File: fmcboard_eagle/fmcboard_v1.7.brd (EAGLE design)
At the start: 147 x 74 mm, 294 parts, among them IC1 OPA699ID, IC10 LM358, IC11 7805DT, IC12 SN74AUC2G66DCTR, IC13 SN74AUC2G66DCTR, IC14 SN74AUC2G66DCTR, IC15 SN74AUC2G66DCTR, IC16 DAC7578SPWR, IC17 SN74AUC2G66DCTR, IC18 SN74AUC2G66DCTR, IC19 SN74AUC2G66DCTR, IC2 DAC7578SPWR, IC20 SN74AUC2G66DCTR, IC21 74AUP2GU04GW, IC22 74AUP2GU04GW, IC23 74AUP2GU04GW, IC24 74AUP2GU04GW, IC25 MC7905ACD2TR4G, IC26 AMS1117-1.8, IC27 LM358, IC28 SN74AUC2G66DCTR, IC29 LM337KVURG3, IC3 LTC6229IMS8E#TRPBF, IC30 SN74AUC2G66DCTR, IC31 SN74AUC2G66DCTR, IC32 SN74AUC2G66DCTR, IC33 LTC6229IMS8E#TRPBF, IC34 74AUP2GU04GW, IC35 74AUP2GU04GW, IC36 TPS5430DDAR, IC37 TPS5430DDAR, IC38 LTC6229IMS8E#TRPBF, IC4 OPA695IDR, IC5 LTC6229IMS8E#TRPBF, IC6 OPA695IDR, IC7 OPA699ID, IC8 LM358, IC9 LM358, J1 4p-2.54, J13 4p-2.54, J2 ASP-134604-01, J3 2X4P-2.54, J4 2X4P-2.54, J5 4p-2.54

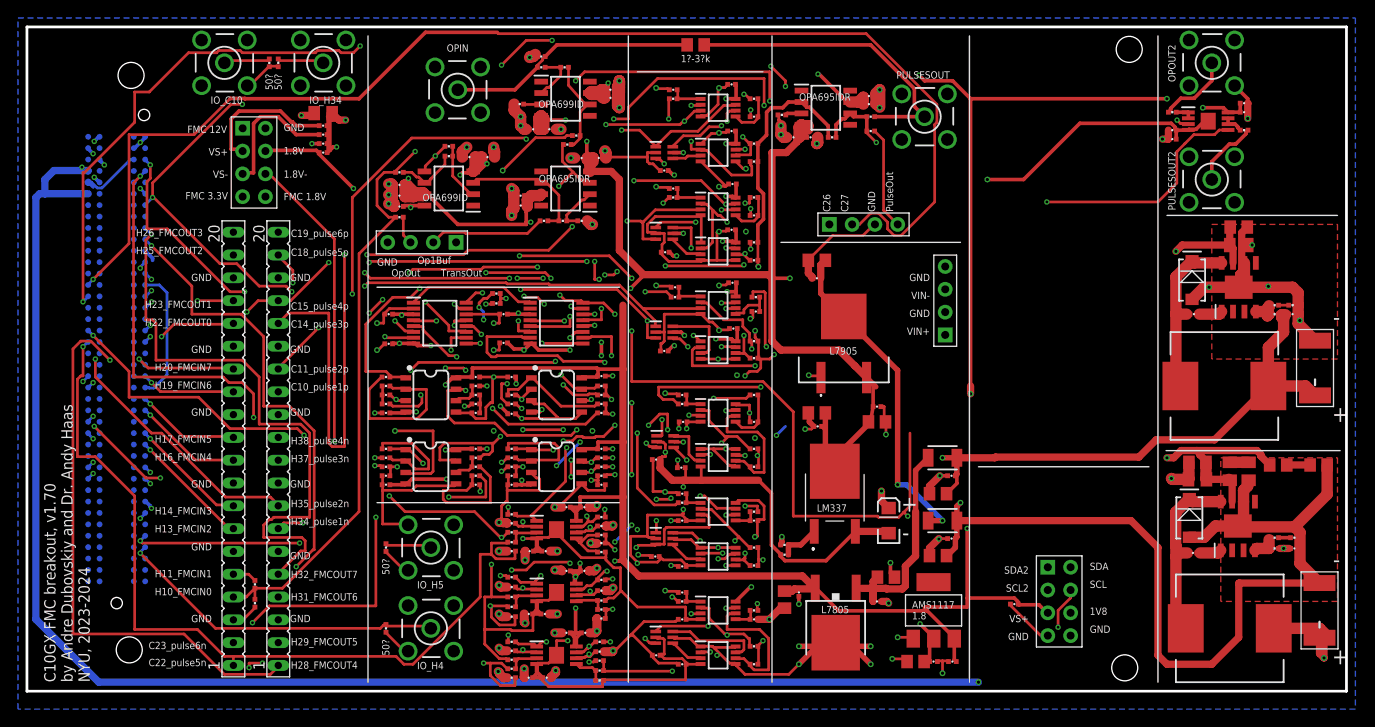
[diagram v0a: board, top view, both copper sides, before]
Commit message: add level shifting
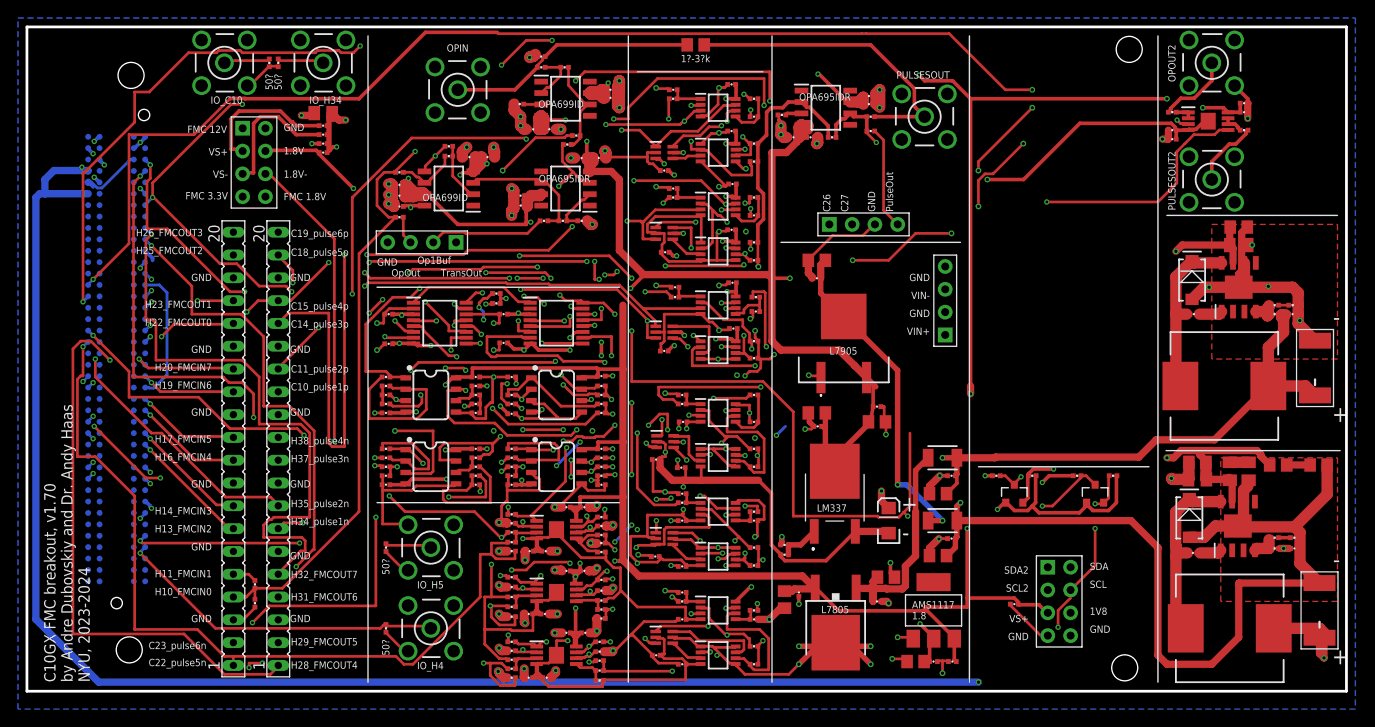
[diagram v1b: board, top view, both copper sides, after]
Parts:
- added R48, R49, R50, R51: 10k, passives:0402_RES
- added U$1, U$2: N-CHANNEL-MOSFET-BSS138, GeekAmmo:SOT23-3
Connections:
- removed net AR_SCLIN2: IC16.16, IC2.16, J4.2
- removed net AR_SDAIN2: IC16.15, IC2.15, J4.1
- new net SCLIN2: IC16.16, IC2.16, J4.2, R51.2, U$2.3
- new net SDAIN2: IC16.15, IC2.15, J4.1, R49.2, U$1.3
- net 1V8: now also R48.1, R50.1, U$1.1, U$2.1
- net SCLIN: now also R50.2, U$2.2
- net SDAIN: now also R48.2, U$1.2
- net VS+: now also R49.1, R51.1
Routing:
- net SDAIN2: track 0.00 -> 142.1 mm, vias 0 -> 5
- net AR_SDAIN2: track 135.9 -> 0.00 mm, vias 4 -> 0
- net SCLIN2: track 0.00 -> 119.7 mm, vias 0 -> 8
- net AR_SCLIN2: track 100.5 -> 0.00 mm, vias 7 -> 0
- net C26: track 121.3 -> 163.9 mm, vias 4 -> 6
- net 1V8: track 227.5 -> 267.8 mm, vias 20 -> 21
- net SDAIN: track 127.5 -> 145.7 mm, vias 1 -> 2
- net C27: track 140.4 -> 155.8 mm, vias 1 -> 4
- net SCLIN: track 123.9 -> 138.9 mm, vias 4 -> 6
- net VS+: track 421.7 -> 436.5 mm, vias 17 -> 19

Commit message: caps
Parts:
- added C118: 0.1uF, passives:0402_CAP
- moved C6 12.6 mm to (107.3, 22.0), turned to 270 degrees
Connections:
- net 1V8: now also C118.1
- net GND: now also C118.2
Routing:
- net GND: track 547.7 -> 544.3 mm, vias 126 -> 128
- net 1V8: track 267.8 -> 269.7 mm
- net VS+: track 436.5 -> 437.7 mm
- net SCLIN: track 138.9 -> 139.5 mm
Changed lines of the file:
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@@
 <attribute name="OC_NEWARK" value="unknown" x="100" y="64" size="0.8128" layer="27" display="off"/>
 </element>
-<element name="C6" library="passives" package="0402_CAP" value="0.1uF" x="110" y="9.7" smashed="yes" rot="R180"/>
+<element name="C6" library="passives" package="0402_CAP" value="0.1uF" x="107.3" y="22" smashed="yes" rot="R270"/>
 <element name="C15" library="passives" package="0402_CAP" value="0.1uF" x="54" y="35" smashed="yes" rot="R180"/>
 <element name="C16" library="passives" package="0402_CAP" value="0.1uF" x="93.8" y="66.3" smashed="yes"/>
@@
 <element name="R50" library="passives" package="0402_RES" value="10k" x="121" y="24" smashed="yes" rot="R180"/>
 <element name="R51" library="passives" package="0402_RES" value="10k" x="117" y="24" smashed="yes"/>
+<element name="C118" library="passives" package="0402_CAP" value="0.1uF" x="123" y="22" smashed="yes" rot="R270"/>
 </elements>
 <signals>
@@
 <contactref element="J4" pad="4"/>
 <contactref element="J4" pad="5"/>
-<wire x1="109.625" y1="9.5" x2="109.625" y2="9.625" width="0.3048" layer="1"/>
-<wire x1="112.875" y1="6.25" x2="109.625" y2="9.5" width="0.3048" layer="1"/>
-<wire x1="113.625" y1="6.25" x2="112.875" y2="6.25" width="0.3048" layer="1"/>
-<wire x1="109.625" y1="9.625" x2="109.56693125" y2="9.7" width="0.3048" layer="1"/>
-<wire x1="113.625" y1="6.25" x2="113.73" y2="6.19" width="0.3048" layer="1"/>
 <wire x1="89.75" y1="50.75" x2="87.25" y2="48.25" width="0.3048" layer="1"/>
 <wire x1="93.125" y1="50.75" x2="89.75" y2="50.75" width="0.3048" layer="1"/>
@@
 <wire x1="87.25" y1="48.25" x2="87.05" y2="48" width="0.3048" layer="1"/>
 <wire x1="94.375" y1="52" x2="94.47" y2="52" width="0.3048" layer="1"/>
+<contactref element="C118" pad="2"/>
+<via x="122.5" y="20.7" extent="1-16" drill="0.35"/>
+<via x="106.5" y="20.7" extent="1-16" drill="0.35"/>
+<wire x1="106.5" y1="20.7" x2="107.3" y2="21.5" width="0.4064" layer="1"/>
+<wire x1="107.3" y1="21.5" x2="107.3" y2="21.56693125" width="0.4064" layer="1"/>
+<wire x1="122.5" y1="20.7" x2="123" y2="21.2" width="0.4064" layer="1"/>
+<wire x1="123" y1="21.2" x2="123" y2="21.56693125" width="0.4064" layer="1"/>
 </signal>
 <signal name="IO1">
@@
 <wire x1="26.65" y1="60.25" x2="32.25" y2="60.25" width="0.4064" layer="1"/>
 <contactref element="J4" pad="6"/>
-<wire x1="115.125" y1="8.625" x2="116.25" y2="8.625" width="0.4064" layer="15"/>
-<wire x1="114.125" y1="7.625" x2="115.125" y2="8.625" width="0.4064" layer="15"/>
-<wire x1="99.625" y1="7.625" x2="114.125" y2="7.625" width="0.4064" layer="15"/>
+<wire x1="115.425" y1="8.625" x2="116.25" y2="8.625" width="0.4064" layer="15"/>
+<wire x1="114.325" y1="7.525" x2="115.425" y2="8.625" width="0.4064" layer="15"/>
+<wire x1="99.525" y1="7.525" x2="114.325" y2="7.525" width="0.4064" layer="15"/>
 <wire x1="116.25" y1="8.625" x2="116.27" y2="8.73" width="0.4064" layer="15"/>
-<wire x1="99.625" y1="7.625" x2="99.5" y2="7.5" width="0.4064" layer="15"/>
+<wire x1="99.525" y1="7.525" x2="99.5" y2="7.5" width="0.4064" layer="15"/>
 <contactref element="R48" pad="1"/>
 <contactref element="U$1" pad="1"/>
@@
 <wire x1="112.375" y1="24" x2="112.43306875" y2="24" width="0.4064" layer="1"/>
 <wire x1="109.125" y1="21" x2="109.05" y2="21" width="0.4064" layer="1"/>
-<wire x1="121.375" y1="21" x2="121.375" y2="24" width="0.4064" layer="1"/>
+<wire x1="121.375" y1="21" x2="121.375" y2="23" width="0.4064" layer="1"/>
+<wire x1="121.375" y1="23" x2="121.375" y2="24" width="0.4064" layer="1"/>
 <wire x1="120.5" y1="20.125" x2="121.375" y2="21" width="0.4064" layer="1"/>
 <wire x1="118.75" y1="20.125" x2="120.5" y2="20.125" width="0.4064" layer="1"/>
@@
 <wire x1="93" y1="20.25" x2="92.875" y2="20.125" width="0.4064" layer="15"/>
 <via x="108.125" y="20.25" extent="1-16" drill="0.3048"/>
+<contactref element="C118" pad="1"/>
+<wire x1="123" y1="22.43306875" x2="121.94193125" y2="22.43306875" width="0.4064" layer="1"/>
+<wire x1="121.94193125" y1="22.43306875" x2="121.375" y2="23" width="0.4064" layer="1"/>
 </signal>
 <signal name="3V3" class="1" airwireshidden="yes">
@@
 <wire x1="104.85" y1="23.125" x2="104.85" y2="24" width="0.4064" layer="15"/>
 <wire x1="104.85" y1="24" x2="104.85" y2="32.85" width="0.4064" layer="15"/>
-<wire x1="104.75" y1="9.375" x2="104.75" y2="10.375" width="0.4064" layer="1"/>
-<wire x1="104.75" y1="10.375" x2="104.75" y2="18.125" width="0.4064" layer="1"/>
+<wire x1="104.75" y1="9.375" x2="104.75" y2="18.125" width="0.4064" layer="1"/>
 <wire x1="100.125" y1="9.375" x2="104.75" y2="9.375" width="0.4064" layer="1"/>
 <wire x1="100.125" y1="9.375" x2="100" y2="9.25" width="0.4064" layer="1"/>
@@
 <wire x1="24" y1="60.2" x2="24" y2="60.375" width="0.4064" layer="1"/>
 <contactref element="J4" pad="3"/>
-<wire x1="112.75" y1="9.625" x2="110.5" y2="9.625" width="0.4064" layer="1"/>
-<wire x1="113.625" y1="8.75" x2="112.75" y2="9.625" width="0.4064" layer="1"/>
-<wire x1="110.5" y1="9.625" x2="110.43306875" y2="9.7" width="0.4064" layer="1"/>
-<wire x1="113.625" y1="8.75" x2="113.73" y2="8.73" width="0.4064" layer="1"/>
-<wire x1="110.375" y1="10" x2="110.375" y2="9.875" width="0.4064" layer="1"/>
-<wire x1="110" y1="10.375" x2="110.375" y2="10" width="0.4064" layer="1"/>
-<wire x1="104.75" y1="10.375" x2="110" y2="10.375" width="0.4064" layer="1"/>
-<wire x1="110.375" y1="9.875" x2="110.43306875" y2="9.7" width="0.4064" layer="1"/>
 <contactref element="R49" pad="1"/>
 <contactref element="R51" pad="1"/>
@@
 <via x="106.75" y="24" extent="1-16" drill="0.3048"/>
 <via x="113.125" y="23.25" extent="1-16" drill="0.3048"/>
+<wire x1="113.73" y1="8.73" x2="105.395" y2="8.73" width="0.4064" layer="1"/>
+<wire x1="105.395" y1="8.73" x2="104.75" y2="9.375" width="0.4064" layer="1"/>
+<wire x1="107.3" y1="22.43306875" x2="107.56693125" y2="22.7" width="0.4064" layer="1"/>
+<wire x1="107.56693125" y1="22.7" x2="107.56693125" y2="24" width="0.4064" layer="1"/>
 </signal>
 <signal name="VS-" class="1" airwireshidden="yes">
@@
 <wire x1="114.875" y1="9" x2="116.25" y2="10.375" width="0.3048" layer="1"/>
 <wire x1="114.875" y1="7.125" x2="114.875" y2="9" width="0.3048" layer="1"/>
-<wire x1="114.875" y1="5.875" x2="114.875" y2="7.125" width="0.3048" layer="15"/>
-<wire x1="112.375" y1="3.375" x2="114.875" y2="5.875" width="0.3048" layer="15"/>
-<wire x1="99.375" y1="3.375" x2="112.375" y2="3.375" width="0.3048" layer="15"/>
+<wire x1="114.875" y1="4.875" x2="114.875" y2="7.125" width="0.3048" layer="15"/>
+<wire x1="113.375" y1="3.375" x2="114.875" y2="4.875" width="0.3048" layer="15"/>
+<wire x1="99.375" y1="3.375" x2="113.375" y2="3.375" width="0.3048" layer="15"/>
 <wire x1="97.5" y1="1.5" x2="99.375" y2="3.375" width="0.3048" layer="15"/>
 <wire x1="116.25" y1="11.25" x2="116.27" y2="11.27" width="0.3048" layer="1"/>
@@
 <wire x1="139.8001" y1="41.93955" x2="140.1999" y2="41.93955" width="1.27" layer="1"/>
 <wire x1="138.3" y1="34" x2="132.3" y2="28" width="0.8128" layer="1"/>
-<wire x1="107.90000625" y1="26.0788" x2="107.82120625" y2="26" width="0.8128" layer="1"/>
-<wire x1="107.82120625" y1="26" x2="103.6" y2="26" width="0.8128" layer="1"/>
-<wire x1="123.87759375" y1="26.0788" x2="107.90000625" y2="26.0788" width="0.8128" layer="1"/>
+<wire x1="123.79879375" y1="26" x2="103.6" y2="26" width="0.8128" layer="1"/>
 <wire x1="132.3" y1="28" x2="125.79879375" y2="28" width="0.8128" layer="1"/>
-<wire x1="125.79879375" y1="28" x2="123.87759375" y2="26.0788" width="0.8128" layer="1"/>
+<wire x1="125.79879375" y1="28" x2="123.79879375" y2="26" width="0.8128" layer="1"/>
 <wire x1="139.5" y1="42" x2="139.43306875" y2="42" width="0.4064" layer="1"/>
 <wire x1="139.5" y1="42" x2="139.8001" y2="41.63296875" width="0.4064" layer="1"/>

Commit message: compress board
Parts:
- J4: value 2X4P-2.54 -> 4p-2.54; device Seeed-Connector:H2X4-2.54 -> Seeed-Connector:H4-2.54
- moved J4 125.5 mm to (5.80, 71.9), turned to 90 degrees
- moved C118 88.1 mm to (35.7, 10.4), turned to 0 degrees
- moved R50 87.7 mm to (34.4, 9.90), turned to 270 degrees
- moved U$2 84.4 mm to (35.7, 8.40), turned to 90 degrees
- moved R51 84.4 mm to (34.4, 6.90), turned to 90 degrees
- moved R48 79.9 mm to (34.4, 5.10), turned to 270 degrees
- moved R49 76.8 mm to (34.4, 2.00), turned to 90 degrees
- moved U$1 76.5 mm to (35.7, 3.60), turned to 90 degrees
- moved C6 74.5 mm to (35.7, 1.50), turned to 0 degrees
- moved D1 20.0 mm to (109.8, 45.8)
- moved C107 20.0 mm to (109.9, 15.4)
- moved C108 20.0 mm to (114.0, 24.5)
- moved C109 20.0 mm to (123.9, 25.2)
- moved C11 20.0 mm to (110.4, 23.6)
- moved C112 20.0 mm to (119.4, 25.2)
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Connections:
- net 1V8: no longer J4.6
- net C26: now also J4.1; no longer J13.1
- net C27: now also J4.3; no longer J13.2
- net GND: now also J13.1, J13.2, J4.2; no longer J4.5
- net SCLIN: no longer J4.7
- net SCLIN2: no longer J4.2
- net SDAIN: no longer J4.8
- net SDAIN2: no longer J4.1
- net VS+: no longer J4.3
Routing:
- net C26: track 163.9 -> 31.2 mm, vias 6 -> 1
- net C27: track 155.8 -> 27.3 mm, vias 4 -> 1
- net SDAIN: track 145.7 -> 33.0 mm
- net SCLIN: track 139.5 -> 39.1 mm, vias 6 -> 4
- net SCLIN2: track 119.7 -> 164.5 mm, vias 8 -> 7
- net VS+: track 437.7 -> 393.0 mm, vias 19 -> 18
- net GND: track 544.3 -> 508.7 mm, vias 128 -> 125
- net C14: track 127.8 -> 94.5 mm
- net PULSESUMOUT: track 56.2 -> 31.0 mm
- net VIN+: track 73.9 -> 53.9 mm
- net VS-: track 302.6 -> 283.6 mm
- net VIN-: track 126.7 -> 108.9 mm
- net OPOUT_H10: track 180.2 -> 162.6 mm
- net SDAIN2: track 142.1 -> 126.8 mm, vias 5 -> 8
- net 12V: track 294.7 -> 280.0 mm
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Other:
- board size 147 x 74 mm -> 127 x 74 mm
- board text removed: "1V8"
- board text removed: "SCL"
- board text removed: "SCL2"
- board text removed: "SDA"
- board text removed: "SDA2"

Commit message: add some holes for scl/sda scl2/sda2
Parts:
- added J6: 4p-2.54, Seeed-Connector:H4-2.54
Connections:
- net SCLIN: now also J6.1
- net SCLIN2: now also J6.3
- net SDAIN: now also J6.2
- net SDAIN2: now also J6.4
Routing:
- net SDAIN2: track 126.8 -> 157.2 mm
- net SCLIN: track 39.1 -> 48.6 mm
- net SCLIN2: track 164.5 -> 170.2 mm, vias 7 -> 8
- net SDAIN: track 33.0 -> 38.1 mm
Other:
- board text added: "SCL"
- board text added: "SCL2"
- board text added: "SDA"
- board text added: "SDA2"
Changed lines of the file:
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@@
 <drawing>
 <settings>
-<setting alwaysvectorfont="yes"/>
+<setting alwaysvectorfont="no"/>
 <setting verticaltext="up"/>
 </settings>
@@
 <text x="22.3" y="63" size="0.8128" layer="21" rot="R180">FMC 12V</text>
 <text x="100.6" y="46.5" size="0.8128" layer="21" rot="R180">GND</text>
-<text x="7" y="1" size="1.27" layer="21" rot="R90">C10GX FMC breakout, v1.70
+<text x="7" y="24" size="1.27" layer="21" rot="R90">C10GX FMC breakout, v1.70
 by Andre Dubovskiy and Dr. Andy Haas
 NYU, 2023-2024</text>
@@
 <text x="6.8" y="67.6" size="0.8128" layer="21" rot="R90">C27</text>
 <text x="8.8" y="67.6" size="0.8128" layer="21" rot="R90">GND</text>
+<text x="8.4" y="17.8" size="0.8128" layer="21" rot="R180">SDA</text>
+<text x="8.4" y="19.8" size="0.8128" layer="21" rot="R180">SCL</text>
+<text x="8.4" y="14.8" size="0.8128" layer="21" rot="R180">SCL2</text>
+<text x="8.4" y="12.8" size="0.8128" layer="21" rot="R180">SDA2</text>
 </plain>
 <attributes>
@@
 <attribute name="MPN" value="F185-1104A1BSYA1" x="-5.2" y="64.9" size="1.778" layer="27" rot="R90" display="off"/>
 </element>
+<element name="J6" library="Seeed-Connector" library_urn="urn:adsk.eagle:library:478" package="H4-2.54" package3d_urn="urn:adsk.eagle:package:33137/1" value="4p-2.54" x="10" y="16.4" smashed="yes">
+<attribute name="MPN" value="F185-1104A1BSYA1" x="10" y="16.4" size="1.778" layer="27" display="off"/>
+</element>
 </elements>
 <signals>
@@
 <via x="14" y="20.25" extent="1-16" drill="0.3048"/>
 <via x="33.5" y="4.375" extent="1-16" drill="0.3048"/>
+<contactref element="J6" pad="2"/>
+<wire x1="10.125" y1="17.75" x2="10.05" y2="17.75" width="0.4064" layer="15"/>
+<wire x1="12.375" y1="20" x2="10.125" y2="17.75" width="0.4064" layer="15"/>
+<wire x1="13.875" y1="20" x2="12.375" y2="20" width="0.4064" layer="15"/>
+<wire x1="10.05" y1="17.75" x2="10" y2="17.67" width="0.4064" layer="15"/>
+<wire x1="13.875" y1="20" x2="14" y2="20.25" width="0.4064" layer="15"/>
 </signal>
 <signal name="H13">
@@
 <wire x1="36.75" y1="9.25" x2="36.7" y2="9.35" width="0.3048" layer="1"/>
 <wire x1="12.625" y1="17.625" x2="12.625" y2="19.25" width="0.3048" layer="15"/>
-<wire x1="21.75" y1="8.5" x2="12.625" y2="17.625" width="0.3048" layer="15"/>
+<wire x1="21.75" y1="8.5" x2="14.0625" y2="16.1875" width="0.3048" layer="15"/>
+<wire x1="14.0625" y1="16.1875" x2="12.625" y2="17.625" width="0.3048" layer="15"/>
 <wire x1="21.75" y1="6.375" x2="21.75" y2="8.5" width="0.3048" layer="15"/>
 <wire x1="31.25" y1="6.375" x2="21.75" y2="6.375" width="0.3048" layer="1"/>
@@
 <via x="12.625" y="19.25" extent="1-16" drill="0.3048"/>
 <via x="21.75" y="6.375" extent="1-16" drill="0.3048"/>
+<contactref element="J6" pad="1"/>
+<wire x1="9.625" y1="19" x2="9.625" y2="19.785" width="0.3048" layer="15"/>
+<wire x1="8.625" y1="18" x2="9.625" y2="19" width="0.3048" layer="15"/>
+<wire x1="8.625" y1="17.25" x2="8.625" y2="18" width="0.3048" layer="15"/>
+<wire x1="9.75" y1="16.125" x2="8.625" y2="17.25" width="0.3048" layer="15"/>
+<wire x1="14" y1="16.125" x2="9.75" y2="16.125" width="0.3048" layer="15"/>
+<wire x1="9.625" y1="19.785" x2="10" y2="20.21" width="0.3048" layer="15"/>
+<wire x1="14" y1="16.125" x2="14.0625" y2="16.1875" width="0.3048" layer="15"/>
 </signal>
 <signal name="H5" airwireshidden="yes">
@@
 <wire x1="9.375" y1="1.375" x2="28.5" y2="1.375" width="0.3048" layer="1"/>
 <wire x1="4.625" y1="6.125" x2="9.375" y2="1.375" width="0.3048" layer="1"/>
-<wire x1="4.625" y1="41" x2="4.625" y2="6.125" width="0.3048" layer="1"/>
+<wire x1="4.625" y1="41" x2="4.625" y2="15.25" width="0.3048" layer="1"/>
+<wire x1="4.625" y1="15.25" x2="4.625" y2="6.125" width="0.3048" layer="1"/>
 <wire x1="9" y1="45.375" x2="4.625" y2="41" width="0.3048" layer="1"/>
 <wire x1="9" y1="53.25" x2="9" y2="45.375" width="0.3048" layer="15"/>
@@
 <via x="56.875" y="49.75" extent="1-16" drill="0.3048"/>
 <via x="54.875" y="49.75" extent="1-16" drill="0.3048"/>
+<contactref element="J6" pad="3"/>
+<wire x1="4.5" y1="15.25" x2="9.925" y2="15.25" width="0.3048" layer="15"/>
+<wire x1="9.925" y1="15.25" x2="10" y2="15.13" width="0.3048" layer="15"/>
+<wire x1="4.5" y1="15.25" x2="4.625" y2="15.25" width="0.3048" layer="1"/>
+<via x="4.5" y="15.25" extent="1-16" drill="0.3048"/>
 </signal>
 <signal name="SDAIN2" airwireshidden="yes">
@@
 <via x="57.625" y="46" extent="1-16" drill="0.3048"/>
 <via x="59.75" y="43.25" extent="1-16" drill="0.3048"/>
+<contactref element="J6" pad="4"/>
+<wire x1="12" y1="12.5" x2="10.05" y2="12.5" width="0.3048" layer="15"/>
+<wire x1="23.125" y1="1.375" x2="12" y2="12.5" width="0.3048" layer="15"/>
+<wire x1="34" y1="1.375" x2="23.125" y2="1.375" width="0.3048" layer="15"/>
+<wire x1="35.125" y1="2.5" x2="34" y2="1.375" width="0.3048" layer="15"/>
+<wire x1="10.05" y1="12.5" x2="10" y2="12.59" width="0.3048" layer="15"/>
+<wire x1="35.125" y1="2.5" x2="35.25" y2="2.5" width="0.3048" layer="15"/>
 </signal>
 <signal name="N$22">
